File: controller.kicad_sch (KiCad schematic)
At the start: 43 parts, among them J1 input_voltage, J10 BOOT0 STATE, J11 GPS, J12 pololu_LV, J13 pololu_HV, J15 MCU_EXTRA2, J16 MCU_EXTRA3, J17 MCU_EXTRA4, J18 NRST, J2 PROGRAMMING CONNECTOR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

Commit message: Dodano układ wejściowy dla zasilania. Nie symulowano całości.
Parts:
- removed J1: input_voltage, Connector_PinSocket_2.54mm:PinSocket_1x02_P2.54mm_Vertical, symbol Connector:Conn_01x02_Socket
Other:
- note removed: "input: 4.75 - 5.25V"
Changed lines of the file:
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@@
 	(wire
 		(pts
-			(xy 26.67 27.94) (xy 26.67 31.75)
-		)
-		(stroke
-			(width 0)
-			(type default)
-		)
-	)
-	(wire
-		(pts
 			(xy 64.77 111.76) (xy 83.82 111.76)
 		)
@@
 	(wire
 		(pts
-			(xy 24.13 27.94) (xy 24.13 31.75)
-		)
-		(stroke
-			(width 0)
-			(type default)
-		)
-	)
-	(wire
-		(pts
 			(xy 140.97 60.96) (xy 138.43 60.96)
 		)
@@
 	(wire
 		(pts
-			(xy 21.59 52.07) (xy 35.56 52.07)
+			(xy 16.51 16.51) (xy 30.48 16.51)
 		)
 		(stroke
@@
 		)
 	)
-	(text "input:\n4.75 - 5.25V"
-		(exclude_from_sim no)
-		(at 13.716 20.32 0)
-		(effects
-			(font
-				(size 1.27 1.27)
-			)
-			(justify left)
-		)
-	)
 	(text "UWAGA\nKondensatory C3, C4\nmuszą być chipa tak blisko jak sie da!"
 		(exclude_from_sim no)
@@
 	)
 	(label "+5v_supply"
-		(at 22.86 52.07 0)
+		(at 17.78 16.51 0)
 		(fields_autoplaced yes)
 		(effects
@@
 	(hierarchical_label "+5v_supply"
 		(shape output)
-		(at 35.56 52.07 0)
+		(at 30.48 16.51 0)
 		(fields_autoplaced yes)
 		(effects
@@
 	)
 	(symbol
-		(lib_id "power:GND")
-		(at 24.13 31.75 0)
-		(unit 1)
-		(exclude_from_sim no)
-		(in_bom yes)
-		(on_board yes)
-		(dnp no)
-		(fields_autoplaced yes)
-		(property "Reference" "#PWR01"
-			(at 24.13 38.1 0)
-			(effects
-				(font
-					(size 1.27 1.27)
-				)
-				(hide yes)
-			)
-		)
-		(property "Value" "GND"
-			(at 24.13 36.83 0)
-			(effects
-				(font
-					(size 1.27 1.27)
-				)
-			)
-		)
-		(property "Footprint" ""
-			(at 24.13 31.75 0)
-			(effects
-				(font
-					(size 1.27 1.27)
-				)
-				(hide yes)
-			)
-		)
-		(property "Datasheet" ""
-			(at 24.13 31.75 0)
-			(effects
-				(font
-					(size 1.27 1.27)
-				)
-				(hide yes)
-			)
-		)
-		(property "Description" "Power symbol creates a global label with name \"GND\" , ground"
-			(at 24.13 31.75 0)
-			(effects
-				(font
-					(size 1.27 1.27)
-				)
-				(hide yes)
-			)
-		)
-		(pin "1"
-		)
-		(instances
-			(project ""
-				(path "/ade9c7e9-87ec-416b-ada9-3e894081f6ea/4c99e6c3-3738-4bcf-bafc-d6e867d37158"
-					(reference "#PWR01")
-					(unit 1)
-				)
-			)
-		)
-	)
-	(symbol
 		(lib_id "Connector:Conn_01x04_Pin")
 		(at 63.5 85.09 180)
@@
 					(unit 1)
 				)
-			)
-		)
-	)
-	(symbol
-		(lib_id "Connector:Conn_01x02_Socket")
-		(at 24.13 22.86 90)
-		(unit 1)
-		(exclude_from_sim no)
-		(in_bom yes)
-		(on_board yes)
-		(dnp no)
-		(fields_autoplaced yes)
-		(property "Reference" "J1"
-			(at 27.94 22.2249 90)
-			(effects
-				(font
-					(size 1.27 1.27)
-				)
-				(justify right)
-			)
-		)
-		(property "Value" "input_voltage"
-			(at 27.94 24.7649 90)
-			(effects
-				(font
-					(size 1.27 1.27)
-				)
-				(justify right)
-			)
-		)
-		(property "Footprint" "Connector_PinSocket_2.54mm:PinSocket_1x02_P2.54mm_Vertical"
-			(at 24.13 22.86 0)
-			(effects
-				(font
-					(size 1.27 1.27)
-				)
-				(hide yes)
-			)
-		)
-		(property "Datasheet" "~"
-			(at 24.13 22.86 0)
-			(effects
-				(font
-					(size 1.27 1.27)
-				)
-				(hide yes)
-			)
-		)
-		(property "Description" "Generic connector, single row, 01x02, script generated"
-			(at 24.13 22.86 0)
-			(effects
-				(font
-					(size 1.27 1.27)
-				)
-				(hide yes)
-			)
-		)
-		(pin "1"
-		)
-		(pin "2"
-		)
-		(instances
-			(project ""
-				(path "/ade9c7e9-87ec-416b-ada9-3e894081f6ea/4c99e6c3-3738-4bcf-bafc-d6e867d37158"
-					(reference "J1")
-					(unit 1)
-				)

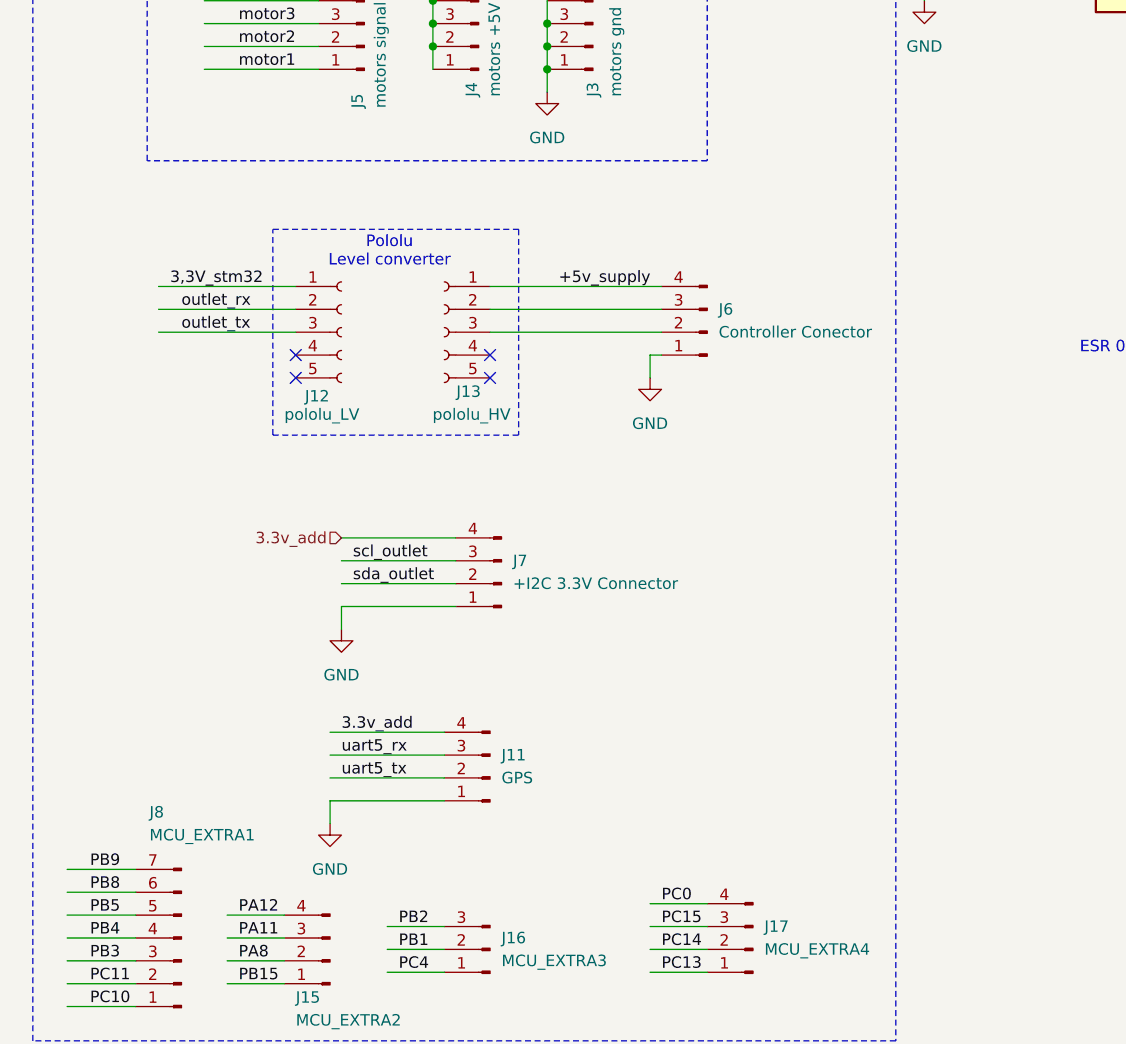
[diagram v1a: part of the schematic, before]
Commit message: Zamieniono konwerter napięć na SMD. Zaktualizowano projekt PCB. Usunięto błedy - zostało część ostrzeżeń dotyczących nakładających się silk.
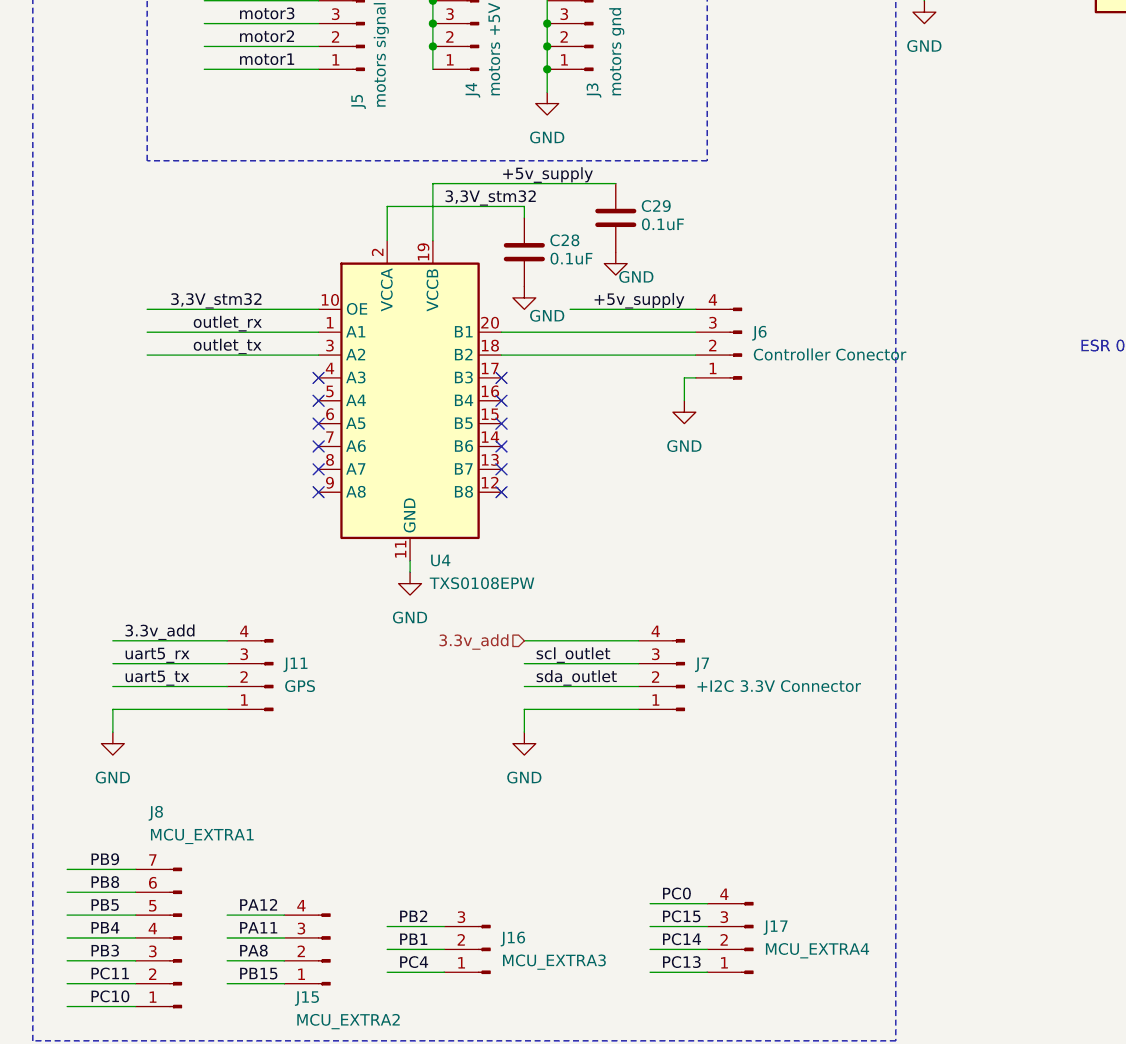
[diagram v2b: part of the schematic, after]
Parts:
- removed J12: pololu_LV, Connector_PinHeader_2.54mm:PinHeader_1x05_P2.54mm_Vertical, symbol Connector:Conn_01x05_Socket
- removed J13: pololu_HV, Connector_PinHeader_2.54mm:PinHeader_1x05_P2.54mm_Vertical, symbol Connector:Conn_01x05_Socket
- added C28, C29: 0.1uF, Capacitor_SMD:C_0603_1608Metric, symbol Device:C
- added U4: TXS0108EPW, Package_SO:TSSOP-20_4.4x6.5mm_P0.65mm, symbol Logic_LevelTranslator:TXS0108EPW
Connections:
- net +5v_supply: now also C29.1, U4.19 (VCCB)
- net 3,3V_stm32: now also C28.1, U4.10 (OE), U4.2 (VCCA)
- net GND: now also C28.2, C29.2, U4.11 (GND)
- net outlet_rx: now also U4.1 (A1)
- net outlet_tx: now also U4.3 (A2)
- net at J6.2 (Pin_2): now also U4.18 (B2)
- net at J6.3 (Pin_3): now also U4.20 (B1)
- no-connect marks 7 -> 15
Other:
- note removed: "Pololu Level converter"
- moved on the sheet: J11, J6, J7

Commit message: dodano komentarze do projektu
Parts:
- added R16: 10k, Resistor_SMD:R_0603_1608Metric, symbol Device:R
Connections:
- net 3,3V_stm32: now also R16.1
- net at C4.1, J18.1 (Pin_1), S1.2 (NO_2)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: now also R16.2
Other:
- note removed: "UWAGA Kondensatory C3, C4 muszą być chipa tak blisko jak sie da!"
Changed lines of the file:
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@@
 	)
 	(junction
+		(at 138.43 48.26)
+		(diameter 0)
+		(color 0 0 0 0)
+	)
+	(junction
 		(at 247.65 22.86)
 		(diameter 0)
@@
 	(wire
 		(pts
+			(xy 138.43 46.99) (xy 138.43 48.26)
+		)
+		(stroke
+			(width 0)
+			(type default)
+		)
+	)
+	(wire
+		(pts
 			(xy 33.02 85.09) (xy 45.72 85.09)
 		)
@@
 	(wire
 		(pts
+			(xy 138.43 39.37) (xy 138.43 35.56)
+		)
+		(stroke
+			(width 0)
+			(type default)
+		)
+	)
+	(wire
+		(pts
 			(xy 59.69 39.37) (xy 59.69 41.91)
 		)
@@
 	(wire
 		(pts
+			(xy 129.54 35.56) (xy 138.43 35.56)
+		)
+		(stroke
+			(width 0)
+			(type default)
+		)
+	)
+	(wire
+		(pts
 			(xy 186.69 43.18) (xy 186.69 38.1)
 		)
@@
 	)
 	(rectangle
-		(start 124.46 26.67)
-		(end 163.83 36.83)
-		(stroke
-			(width 0)
-			(type default)
-		)
-		(fill
-			(type none)
-		)
-	)
-	(rectangle
 		(start 209.55 45.72)
 		(end 232.41 53.34)
@@
 		)
 	)
-	(text "UWAGA\nKondensatory C3, C4\nmuszą być chipa tak blisko jak sie da!"
-		(exclude_from_sim no)
-		(at 144.526 31.75 0)
-		(effects
-			(font
-				(size 1.27 1.27)
-			)
-		)
-	)
 	(text "UART4\n+RTS/CTS"
 		(exclude_from_sim no)
@@
 		)
 	)
+	(label "3,3V_stm32"
+		(at 130.81 35.56 0)
+		(fields_autoplaced yes)
+		(effects
+			(font
+				(size 1.27 1.27)
+			)
+			(justify left bottom)
+		)
+	)
 	(label "LED_R"
 		(at 160.02 76.2 180)
@@
 					(unit 1)
 				)
+			)
+		)
+	)
+	(symbol
+		(lib_id "Device:R")
+		(at 138.43 43.18 0)
+		(unit 1)
+		(exclude_from_sim no)
+		(in_bom yes)
+		(on_board yes)
+		(dnp no)
+		(fields_autoplaced yes)
+		(property "Reference" "R16"
+			(at 140.97 41.9099 0)
+			(effects
+				(font
+					(size 1.27 1.27)
+				)
+				(justify left)
+			)
+		)
+		(property "Value" "10k"
+			(at 140.97 44.4499 0)
+			(effects
+				(font
+					(size 1.27 1.27)
+				)
+				(justify left)
+			)
+		)
+		(property "Footprint" "Resistor_SMD:R_0603_1608Metric"
+			(at 136.652 43.18 90)
+			(effects
+				(font
+					(size 1.27 1.27)
+				)
+				(hide yes)
+			)
+		)
+		(property "Datasheet" "~"
+			(at 138.43 43.18 0)
+			(effects
+				(font
+					(size 1.27 1.27)
+				)
+				(hide yes)
+			)
+		)
+		(property "Description" "Resistor"
+			(at 138.43 43.18 0)
+			(effects
+				(font
+					(size 1.27 1.27)
+				)
+				(hide yes)
+			)
+		)
+		(pin "2"
+		)
+		(pin "1"
+		)
+		(instances
+			(project ""
+				(path "/ade9c7e9-87ec-416b-ada9-3e894081f6ea/4c99e6c3-3738-4bcf-bafc-d6e867d37158"
+					(reference "R16")
+					(unit 1)
+				)
